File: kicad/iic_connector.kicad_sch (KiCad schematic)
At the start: 15 parts

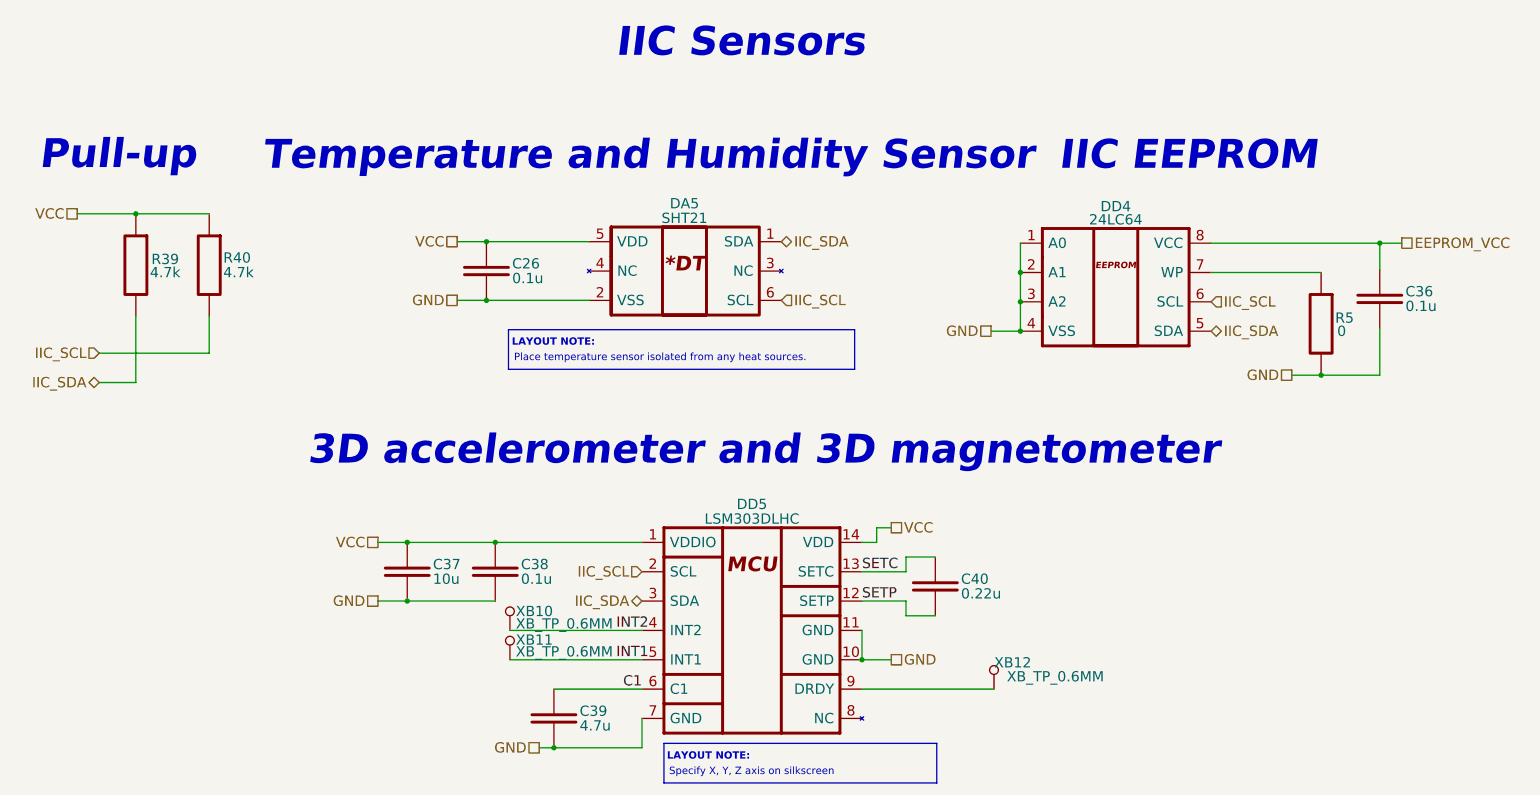
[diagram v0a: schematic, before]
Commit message: Reannotate schematic; Fix 5032 crystal footprint field; Update PCB with 5032 crystal
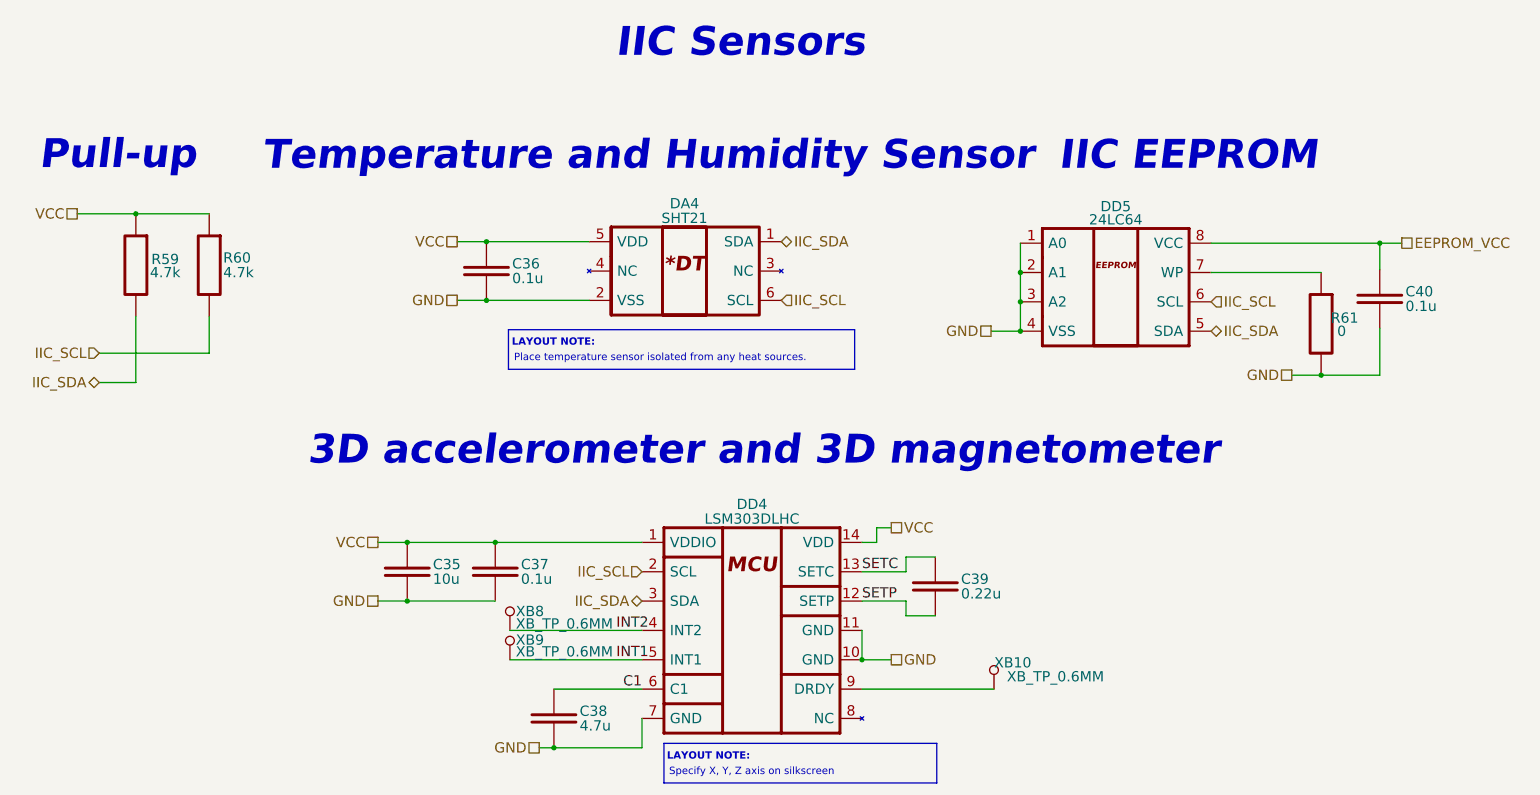
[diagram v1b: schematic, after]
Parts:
- renumbered C37 to C35, C26 to C36, C38 to C37, C39 to C38, C40 to C39, C36 to C40, DA5 to DA4, DD5 to DD4, DD4 to DD5, R39 to R59, R40 to R60, R5 to R61, XB12 to XB10, XB10 to XB8, XB11 to XB9
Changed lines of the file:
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@@
   (symbol (lib_id "Capacitors:C_CAP") (at 107.95 127.254 270) (unit 1)
     (in_bom yes) (on_board yes)
-    (property "Reference" "C38" (id 0) (at 112.395 125.984 90)
+    (property "Reference" "C37" (id 0) (at 112.395 125.984 90)
       (effects (font (size 1.778 1.778)) (justify left))
     )
@@
   (symbol (lib_id "Chips:SHT21") (at 140.716 67.564 0) (unit 1)
     (in_bom yes) (on_board yes)
-    (property "Reference" "DA5" (id 0) (at 140.716 63.5 0)
+    (property "Reference" "DA4" (id 0) (at 140.716 63.5 0)
       (effects (font (size 1.778 1.778)))
     )
@@
   (symbol (lib_id "Chips:24LC64") (at 215.392 77.978 0) (unit 1)
     (in_bom yes) (on_board yes)
-    (property "Reference" "DD4" (id 0) (at 215.392 64.008 0)
+    (property "Reference" "DD5" (id 0) (at 215.392 64.008 0)
       (effects (font (size 1.778 1.778)))
     )
@@
   (symbol (lib_id "Capacitors:C_CAP") (at 184.15 129.794 270) (unit 1)
     (in_bom yes) (on_board yes)
-    (property "Reference" "C40" (id 0) (at 188.595 128.524 90)
+    (property "Reference" "C39" (id 0) (at 188.595 128.524 90)
       (effects (font (size 1.778 1.778)) (justify left))
     )
@@
   (symbol (lib_id "Capacitors:C_CAP") (at 92.71 127.254 270) (unit 1)
     (in_bom yes) (on_board yes)
-    (property "Reference" "C37" (id 0) (at 97.155 125.984 90)
+    (property "Reference" "C35" (id 0) (at 97.155 125.984 90)
       (effects (font (size 1.778 1.778)) (justify left))
     )
@@
   (symbol (lib_id "Resistors:R_RES") (at 58.42 74.168 270) (unit 1)
     (in_bom yes) (on_board yes)
-    (property "Reference" "R40" (id 0) (at 63.246 72.898 90)
+    (property "Reference" "R60" (id 0) (at 63.246 72.898 90)
       (effects (font (size 1.778 1.778)))
     )
@@
   (symbol (lib_id "Connectors:XB_TP_0.6MM") (at 110.49 137.414 0) (unit 1)
     (in_bom no) (on_board yes)
-    (property "Reference" "XB10" (id 0) (at 111.506 134.112 0)
+    (property "Reference" "XB8" (id 0) (at 111.506 134.112 0)
       (effects (font (size 1.778 1.778)) (justify left))
     )
@@
   (symbol (lib_id "Resistors:R_RES") (at 250.952 84.328 270) (unit 1)
     (in_bom yes) (on_board yes)
-    (property "Reference" "R5" (id 0) (at 255.016 83.312 90)
+    (property "Reference" "R61" (id 0) (at 255.016 83.312 90)
       (effects (font (size 1.778 1.778)))
     )
@@
   (symbol (lib_id "Connectors:XB_TP_0.6MM") (at 110.49 142.494 0) (unit 1)
     (in_bom no) (on_board yes)
-    (property "Reference" "XB11" (id 0) (at 111.506 139.065 0)
+    (property "Reference" "XB9" (id 0) (at 111.506 139.065 0)
       (effects (font (size 1.778 1.778)) (justify left))
     )
@@
   (symbol (lib_id "Resistors:R_RES") (at 45.72 74.168 270) (unit 1)
     (in_bom yes) (on_board yes)
-    (property "Reference" "R39" (id 0) (at 50.8 73.152 90)
+    (property "Reference" "R59" (id 0) (at 50.8 73.152 90)
       (effects (font (size 1.778 1.778)))
     )
@@
   (symbol (lib_id "Connectors:XB_TP_0.6MM") (at 194.31 147.574 0) (mirror y) (unit 1)
     (in_bom no) (on_board yes)
-    (property "Reference" "XB12" (id 0) (at 200.787 143.002 0)
+    (property "Reference" "XB10" (id 0) (at 200.787 143.002 0)
       (effects (font (size 1.778 1.778)) (justify left))
     )
@@
   (symbol (lib_id "Capacitors:C_CAP") (at 106.426 75.184 270) (unit 1)
     (in_bom yes) (on_board yes)
-    (property "Reference" "C26" (id 0) (at 110.871 73.914 90)
+    (property "Reference" "C36" (id 0) (at 110.871 73.914 90)
       (effects (font (size 1.778 1.778)) (justify left))
     )
@@
   (symbol (lib_id "Chips:LSM303DLHC") (at 152.4 129.794 0) (unit 1)
     (in_bom yes) (on_board yes)
-    (property "Reference" "DD5" (id 0) (at 152.4 115.57 0)
+    (property "Reference" "DD4" (id 0) (at 152.4 115.57 0)
       (effects (font (size 1.778 1.778)))
     )
@@
   (symbol (lib_id "Capacitors:C_CAP") (at 118.11 152.654 270) (unit 1)
     (in_bom yes) (on_board yes)
-    (property "Reference" "C39" (id 0) (at 122.555 151.384 90)
+    (property "Reference" "C38" (id 0) (at 122.555 151.384 90)
       (effects (font (size 1.778 1.778)) (justify left))
     )
@@
   (symbol (lib_id "Capacitors:C_CAP") (at 261.112 80.01 270) (unit 1)
     (in_bom yes) (on_board yes)
-    (property "Reference" "C36" (id 0) (at 265.557 78.74 90)
-      (effects (font (size 1.778 1.778)) (justify left))
-    )
+    (property "Reference" "C40" (id 0) (at 265.557 78.74 90)
+      (effects (font (size 1.778 1.778)) (justify left))
+    )

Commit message: Add voltage value to caps, update BOM, SCH, ASM
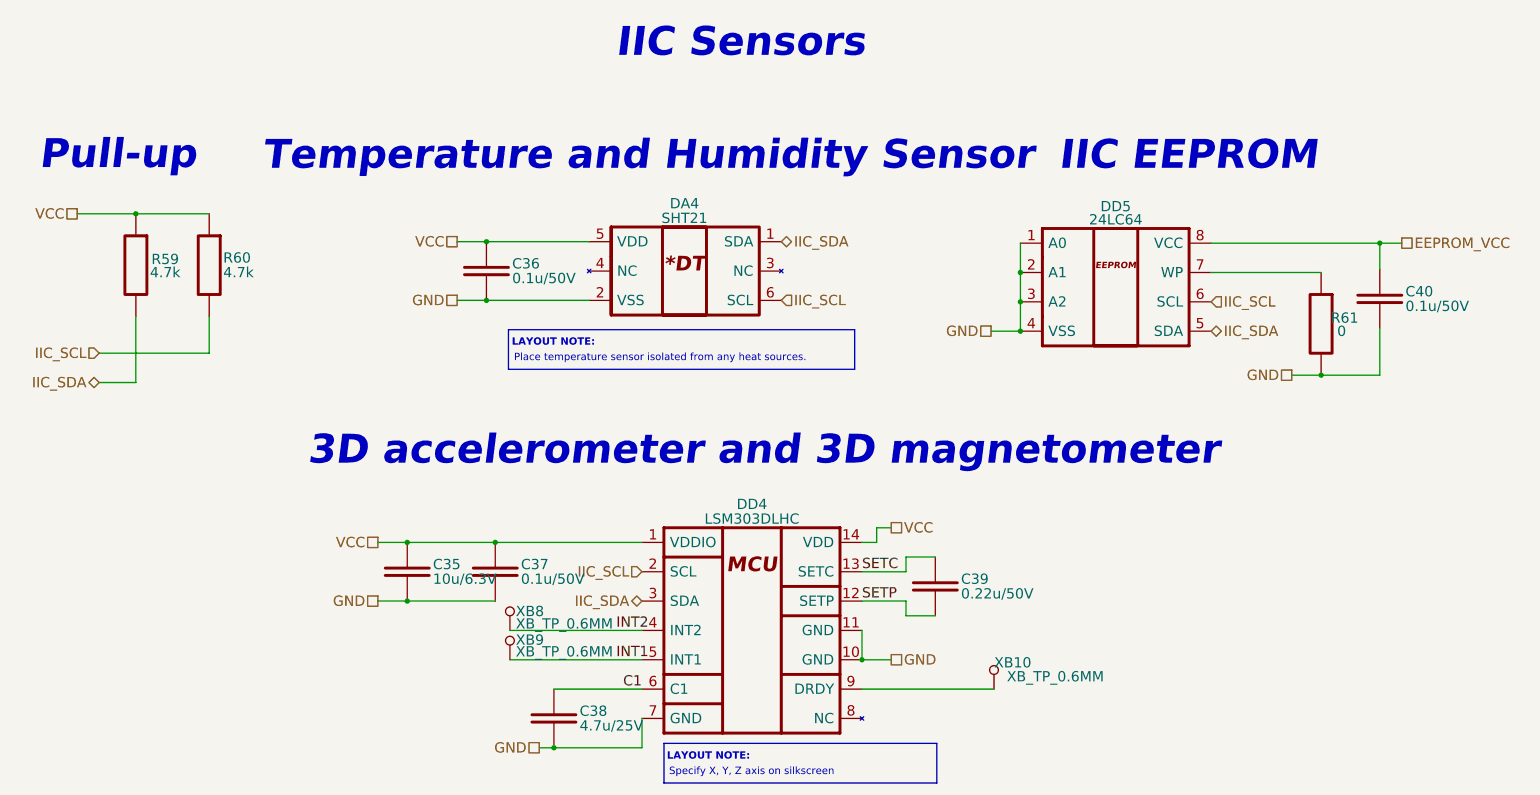
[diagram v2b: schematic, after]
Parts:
- C35: value 10u -> 10u/6.3V; Case/Package (none) -> 0603; Tolerance (none) -> ±10%; Type (none) -> X7R
- C36, C37, C40: value 0.1u -> 0.1u/50V; Tolerance (none) -> ±10%; Type (none) -> X7R
- C38: value 4.7u -> 4.7u/25V; Case/Package (none) -> 0603; Tolerance (none) -> ±10%; Type (none) -> X7R
- C39: value 0.22u -> 0.22u/50V; Case/Package (none) -> 0603; Tolerance (none) -> ±10%; Type (none) -> X7R
- R59, R60, R61: Case/Package 0000 -> 0603; Tolerance ±% -> ±5%
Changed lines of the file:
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@@
     (effects (font (size 1.778 1.778)) (justify left))
   )
-  (symbol (lib_id "Capacitors:C_CAP") (at 107.95 127.254 270) (unit 1)
+  (symbol (lib_name "C_CAP_2") (lib_id "Capacitors:C_CAP") (at 107.95 127.254 270) (unit 1)
     (in_bom yes) (on_board yes)
     (property "Reference" "C37" (id 0) (at 112.395 125.984 90)
       (effects (font (size 1.778 1.778)) (justify left))
     )
-    (property "Value" "0.1u" (id 1) (at 112.395 128.524 90)
+    (property "Value" "0.1u/50V" (id 1) (at 112.395 128.524 90)
       (effects (font (size 1.778 1.778)) (justify left))
     )
@@
     (property "Assembly" "" (id 4) (at 99.06 127.254 0)
       (effects (font (size 1.778 1.778)))
+    )
+    (property "Voltage" "" (id 5) (at 107.95 127.254 0)
+      (effects (font (size 1.27 1.27)) hide)
+    )
+    (property "Case/Package" "" (id 6) (at 107.95 127.254 0)
+      (effects (font (size 1.27 1.27)) hide)
+    )
+    (property "Type" "X7R" (id 7) (at 97.79 127.254 0)
+      (effects (font (size 1.27 1.27)) hide)
+    )
+    (property "Tolerance" "±10%" (id 8) (at 95.25 127.254 0)
+      (effects (font (size 1.27 1.27)) hide)
     )
     (pin "1")
@@
       (effects (font (size 1.778 1.778)) (justify left))
     )
-    (property "Value" "0.22u" (id 1) (at 188.595 131.064 90)
+    (property "Value" "0.22u/50V" (id 1) (at 188.595 131.064 90)
       (effects (font (size 1.778 1.778)) (justify left))
     )
@@
       (effects (font (size 1.778 1.778)))
     )
-    (pin "1")
-    (pin "2")
-  )
-  (symbol (lib_id "Capacitors:C_CAP") (at 92.71 127.254 270) (unit 1)
+    (property "Voltage" "" (id 5) (at 184.15 129.794 0)
+      (effects (font (size 1.27 1.27)) hide)
+    )
+    (property "Case/Package" "0603" (id 6) (at 184.15 129.794 0)
+      (effects (font (size 1.27 1.27)) hide)
+    )
+    (property "Type" "X7R" (id 7) (at 173.99 129.794 0)
+      (effects (font (size 1.27 1.27)) hide)
+    )
+    (property "Tolerance" "±10%" (id 8) (at 171.45 129.794 0)
+      (effects (font (size 1.27 1.27)) hide)
+    )
+    (pin "1")
+    (pin "2")
+  )
+  (symbol (lib_name "C_CAP_4") (lib_id "Capacitors:C_CAP") (at 92.71 127.254 270) (unit 1)
     (in_bom yes) (on_board yes)
     (property "Reference" "C35" (id 0) (at 97.155 125.984 90)
       (effects (font (size 1.778 1.778)) (justify left))
     )
-    (property "Value" "10u" (id 1) (at 97.155 128.524 90)
+    (property "Value" "10u/6.3V" (id 1) (at 97.155 128.524 90)
       (effects (font (size 1.778 1.778)) (justify left))
     )
@@
       (effects (font (size 1.778 1.778)))
     )
-    (pin "1")
-    (pin "2")
-  )
-  (symbol (lib_id "Resistors:R_RES") (at 58.42 74.168 270) (unit 1)
+    (property "Voltage" "" (id 5) (at 92.71 127.254 0)
+      (effects (font (size 1.27 1.27)) hide)
+    )
+    (property "Case/Package" "0603" (id 6) (at 92.71 127.254 0)
+      (effects (font (size 1.27 1.27)) hide)
+    )
+    (property "Type" "X7R" (id 7) (at 82.55 127.254 0)
+      (effects (font (size 1.27 1.27)) hide)
+    )
+    (property "Tolerance" "±10%" (id 8) (at 80.01 127.254 0)
+      (effects (font (size 1.27 1.27)) hide)
+    )
+    (pin "1")
+    (pin "2")
+  )
+  (symbol (lib_name "R_RES_2") (lib_id "Resistors:R_RES") (at 58.42 74.168 270) (unit 1)
     (in_bom yes) (on_board yes)
     (property "Reference" "R60" (id 0) (at 63.246 72.898 90)
@@
       (effects (font (size 1.778 1.778)))
     )
-    (property "Case/Package" "0000" (id 5) (at 52.07 74.168 0)
+    (property "Case/Package" "0603" (id 5) (at 52.07 74.168 0)
       (effects (font (size 1.27 1.27)) hide)
     )
@@
       (effects (font (size 1.27 1.27)) hide)
     )
-    (property "Tolerance" "±%" (id 7) (at 48.768 74.168 0)
-      (effects (font (size 1.27 1.27)) hide)
-    )
+    (property "Tolerance" "±5%" (id 7) (at 48.768 74.168 0)
+      (effects (font (size 1.27 1.27)) hide)
+    )
+    (property "Part Number" "" (id 8) (at 58.42 74.168 0))
     (pin "1")
     (pin "2")
@@
     (pin "1")
   )
-  (symbol (lib_id "Resistors:R_RES") (at 250.952 84.328 270) (unit 1)
+  (symbol (lib_name "R_RES_1") (lib_id "Resistors:R_RES") (at 250.952 84.328 270) (unit 1)
     (in_bom yes) (on_board yes)
     (property "Reference" "R61" (id 0) (at 255.016 83.312 90)
@@
       (effects (font (size 1.778 1.778)))
     )
-    (property "Case/Package" "0000" (id 5) (at 244.602 84.328 0)
+    (property "Case/Package" "0603" (id 5) (at 244.602 84.328 0)
       (effects (font (size 1.27 1.27)) hide)
     )
@@
       (effects (font (size 1.27 1.27)) hide)
     )
-    (property "Tolerance" "±%" (id 7) (at 241.3 84.328 0)
-      (effects (font (size 1.27 1.27)) hide)
-    )
+    (property "Tolerance" "±5%" (id 7) (at 241.3 84.328 0)
+      (effects (font (size 1.27 1.27)) hide)
+    )
+    (property "Part Number" "" (id 8) (at 250.952 84.328 0))
     (pin "1")
     (pin "2")
@@
       (effects (font (size 1.778 1.778)))
     )
-    (property "Case/Package" "0000" (id 5) (at 39.37 74.168 0)
+    (property "Case/Package" "0603" (id 5) (at 39.37 74.168 0)
       (effects (font (size 1.27 1.27)) hide)
     )
@@
       (effects (font (size 1.27 1.27)) hide)
     )
-    (property "Tolerance" "±%" (id 7) (at 36.068 74.168 0)
-      (effects (font (size 1.27 1.27)) hide)
-    )
+    (property "Tolerance" "±5%" (id 7) (at 36.068 74.168 0)
+      (effects (font (size 1.27 1.27)) hide)
+    )
+    (property "Part Number" "" (id 8) (at 45.72 74.168 0))
     (pin "1")
     (pin "2")
@@
     (pin "1")
   )
-  (symbol (lib_id "Capacitors:C_CAP") (at 106.426 75.184 270) (unit 1)
+  (symbol (lib_name "C_CAP_3") (lib_id "Capacitors:C_CAP") (at 106.426 75.184 270) (unit 1)
     (in_bom yes) (on_board yes)
     (property "Reference" "C36" (id 0) (at 110.871 73.914 90)
       (effects (font (size 1.778 1.778)) (justify left))
     )
-    (property "Value" "0.1u" (id 1) (at 110.871 76.454 90)
+    (property "Value" "0.1u/50V" (id 1) (at 110.871 76.454 90)
       (effects (font (size 1.778 1.778)) (justify left))
     )
@@
     (property "Assembly" "" (id 4) (at 97.536 75.184 0)
       (effects (font (size 1.778 1.778)))
+    )
+    (property "Voltage" "" (id 5) (at 106.426 75.184 0)
+      (effects (font (size 1.27 1.27)) hide)
+    )
+    (property "Case/Package" "" (id 6) (at 106.426 75.184 0)
+      (effects (font (size 1.27 1.27)) hide)
+    )
+    (property "Type" "X7R" (id 7) (at 96.266 75.184 0)
+      (effects (font (size 1.27 1.27)) hide)
+    )
+    (property "Tolerance" "±10%" (id 8) (at 93.726 75.184 0)
+      (effects (font (size 1.27 1.27)) hide)
     )
     (pin "1")
@@
     (pin "9")
   )
-  (symbol (lib_id "Capacitors:C_CAP") (at 118.11 152.654 270) (unit 1)
+  (symbol (lib_name "C_CAP_5") (lib_id "Capacitors:C_CAP") (at 118.11 152.654 270) (unit 1)
     (in_bom yes) (on_board yes)
     (property "Reference" "C38" (id 0) (at 122.555 151.384 90)
       (effects (font (size 1.778 1.778)) (justify left))
     )
-    (property "Value" "4.7u" (id 1) (at 122.555 153.924 90)
+    (property "Value" "4.7u/25V" (id 1) (at 122.555 153.924 90)
       (effects (font (size 1.778 1.778)) (justify left))
     )
@@
       (effects (font (size 1.778 1.778)))
     )
-    (pin "1")
-    (pin "2")
-  )
-  (symbol (lib_id "Capacitors:C_CAP") (at 261.112 80.01 270) (unit 1)
+    (property "Voltage" "" (id 5) (at 118.11 152.654 0)
+      (effects (font (size 1.27 1.27)) hide)
+    )
+    (property "Case/Package" "0603" (id 6) (at 118.11 152.654 0)
+      (effects (font (size 1.27 1.27)) hide)
+    )
+    (property "Type" "X7R" (id 7) (at 107.95 152.654 0)
+      (effects (font (size 1.27 1.27)) hide)
+    )
+    (property "Tolerance" "±10%" (id 8) (at 105.41 152.654 0)
+      (effects (font (size 1.27 1.27)) hide)
+    )
+    (pin "1")
+    (pin "2")
+  )
+  (symbol (lib_name "C_CAP_1") (lib_id "Capacitors:C_CAP") (at 261.112 80.01 270) (unit 1)
     (in_bom yes) (on_board yes)
     (property "Reference" "C40" (id 0) (at 265.557 78.74 90)
       (effects (font (size 1.778 1.778)) (justify left))
     )
-    (property "Value" "0.1u" (id 1) (at 265.557 81.28 90)
+    (property "Value" "0.1u/50V" (id 1) (at 265.557 81.28 90)
       (effects (font (size 1.778 1.778)) (justify left))
     )
@@
       (effects (font (size 1.778 1.778)) hide)
     )
-    (pin "1")
+    (property "Voltage" "" (id 4) (at 261.112 80.01 0)
+      (effects (font (size 1.27 1.27)) hide)
+    )
+    (property "Case/Package" "" (id 5) (at 261.112 80.01 0)
+      (effects (font (size 1.27 1.27)) hide)
+    )
+    (property "Type" "X7R" (id 6) (at 250.952 80.01 0)
+      (effects (font (size 1.27 1.27)) hide)
+    )
+    (property "Tolerance" "±10%" (id 7) (at 248.412 80.01 0)
+      (effects (font (size 1.27 1.27)) hide)
+    )
+    (property "Assembly" "" (id 8) (at 252.222 80.01 0)
+      (effects (font (size 1.778 1.778)))
+    )
+    (pin "1")
